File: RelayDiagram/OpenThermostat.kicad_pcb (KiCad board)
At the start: 2 copper layers, 152.5 x 101.5 mm, 90 parts, among them J1 Conn_01x08_Female, J2 Conn_01x15_Female, J3 Conn_01x15_Female, J4 Conn_01x09_Female, Q1 Q_NMOS_DGS, Q10 Q_NMOS_DGS, Q11 Q_NMOS_DGS, Q12 Q_NMOS_DGS, Q2 Q_NMOS_DGS, Q3 Q_NMOS_DGS, Q4 Q_NMOS_DGS, Q5 Q_NMOS_DGS, Q6 Q_NMOS_DGS, Q7 Q_NMOS_DGS, Q8 Q_NMOS_DGS, Q9 Q_NMOS_DGS, SW2 SW_Push, SW3 SW_Push, SW4 SW_Push, SW5 SW_Push, SW6 SW_Push, U1 PCF8574, U10 MB10S-13, U11 L7805CV, U2 LCD, U3 DHT11, U4 EE2-3TNU-L_DPDT_Relay, U5 EE2-3TNU-L_DPDT_Relay, U6 EE2-3TNU-L_DPDT_Relay, U7 EE2-3TNU-L_DPDT_Relay, U8 EE2-3TNU-L_DPDT_Relay, U9 EE2-3TNU-L_DPDT_Relay

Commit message: Change
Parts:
- moved R38 8.19 mm to (160.3, 153.9), turned to 90 degrees
- moved Q5 5.71 mm to (163.7, 149.7)
- moved R15 5.54 mm to (165.0, 128.9)
- moved R14 5.20 mm to (163.7, 154.3)
- moved R26 5.20 mm to (163.7, 151.6)
- moved R39 5.07 mm to (165.5, 125.1)
- moved D6 5.03 mm to (161.3, 125.1)
- moved Q6 3.29 mm to (161.0, 128.9), turned to 90 degrees
- moved D5 2.16 mm to (160.3, 149.5), turned to 90 degrees
- moved R27 1.76 mm to (162.8, 128.9), turned to 90 degrees
- moved U6 0.55 mm to (167.4, 145.2)
- moved R35 0.08 mm to (198.6, 129.4)
- moved Q1 0.08 mm to (189.7, 149.2)
- moved Q2 0.08 mm to (189.7, 128.4)
- moved R11 0.08 mm to (194.8, 126.6)
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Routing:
- net GND: track 39.6 -> 34.7 mm, vias 21 -> 18
- net Net-(Q2-Pad2): track 4.75 -> 0.00 mm
- net Net-(Q1-Pad2): track 4.40 -> 0.00 mm
- net Net-(D2-Pad1): track 1.72 -> 0.00 mm
- net Net-(D1-Pad1): track 1.72 -> 0.00 mm
- added copper zone on F.Cu, net +5V
- removed copper zone on F.Cu, net GND
- removed copper zone on F.Cu, net Net-(D1-Pad2)
- removed copper zone on F.Cu, net Net-(D2-Pad2)

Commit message: PCB updates
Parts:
- moved R18 30.4 mm to (129.4, 154.6), turned to 0 degrees
- moved R30 30.0 mm to (129.4, 151.9), turned to 0 degrees
- moved R31 26.0 mm to (128.7, 126.5), turned to 0 degrees
- moved R42 25.7 mm to (125.2, 154.1), turned to 90 degrees
- moved Q9 25.4 mm to (129.7, 149.7), turned to 0 degrees
- moved D12 25.2 mm to (115.8, 124.1), turned to 90 degrees
- moved R40 24.7 mm to (142.7, 153.9), turned to 90 degrees
- moved D10 24.2 mm to (132.8, 125.0), turned to 90 degrees
- moved R43 23.4 mm to (130.8, 129.7), turned to 90 degrees
- moved R19 22.6 mm to (124.3, 126.0), turned to 0 degrees
- moved D11 22.4 mm to (104.4, 149.6), turned to 90 degrees
- moved R41 22.2 mm to (150.1, 127.0)
- moved D9 21.0 mm to (125.2, 149.6), turned to 90 degrees
- moved Q10 20.4 mm to (124.5, 130.8), turned to 0 degrees
- moved U8 15.1 mm to (133.3, 145.2), turned to 90 degrees
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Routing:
- net GND: track 34.7 -> 53.7 mm, vias 18 -> 24
- net Net-(Q9-Pad2): track 0.00 -> 5.06 mm
- net Net-(Q7-Pad2): track 0.00 -> 5.06 mm
- net Net-(Q5-Pad2): track 0.00 -> 5.06 mm
- net Net-(Q3-Pad2): track 0.00 -> 5.06 mm
- net Net-(Q11-Pad2): track 0.00 -> 5.06 mm
- net Net-(Q1-Pad2): track 0.00 -> 4.93 mm
- net Net-(D9-Pad1): track 0.00 -> 1.84 mm
- net Net-(D7-Pad1): track 0.00 -> 1.84 mm
- net Net-(D5-Pad1): track 0.00 -> 1.84 mm
- net Net-(D3-Pad1): track 0.00 -> 1.84 mm
- net Net-(D11-Pad1): track 0.00 -> 1.84 mm
- net Net-(D1-Pad1): track 0.00 -> 1.84 mm
- added copper zone on F.Cu, net GND
- added copper zone on F.Cu, net Net-(D1-Pad2)
- added copper zone on F.Cu, net Net-(D11-Pad2)
- added copper zone on F.Cu, net Net-(D3-Pad2)
- added copper zone on F.Cu, net Net-(D5-Pad2)
- added copper zone on F.Cu, net Net-(D7-Pad2)
- added copper zone on F.Cu, net Net-(D9-Pad2)
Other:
- board text added: "Relays and other components here should stay on a 5 mil grid"

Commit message: relay pcb changes
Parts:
- moved D12 12.0 mm to (104.6, 128.4), turned to 270 degrees
- moved R37 9.25 mm to (175.9, 123.8), turned to 270 degrees
- moved R35 9.14 mm to (191.4, 123.8), turned to 270 degrees
- moved R19 9.08 mm to (133.0, 128.8), turned to 270 degrees
- moved R33 8.22 mm to (110.2, 125.7)
- moved D10 8.13 mm to (125.5, 128.4), turned to 270 degrees
- moved R43 7.91 mm to (125.5, 123.8), turned to 270 degrees
- moved R41 7.79 mm to (143.0, 123.8), turned to 270 degrees
- moved R21 7.65 mm to (112.1, 128.8), turned to 270 degrees
- moved R13 7.57 mm to (183.4, 128.8), turned to 270 degrees
- moved R17 7.49 mm to (150.6, 128.8), turned to 270 degrees
- moved R45 7.03 mm to (104.6, 123.8), turned to 270 degrees
- moved Q8 6.45 mm to (147.4, 128.3)
- moved Q4 6.10 mm to (180.2, 128.1)
- moved Q2 5.97 mm to (195.7, 128.1)
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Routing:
- net GND: track 53.7 -> 68.4 mm, vias 24 -> 30
- net Net-(Q8-Pad2): track 0.00 -> 5.54 mm
- net Net-(Q6-Pad2): track 0.00 -> 5.54 mm
- net Net-(Q4-Pad2): track 0.00 -> 5.49 mm
- net Net-(Q2-Pad2): track 0.00 -> 5.49 mm
- net Net-(Q12-Pad2): track 0.00 -> 5.49 mm
- net Net-(Q10-Pad2): track 0.00 -> 5.49 mm
- net Net-(D8-Pad1): track 0.00 -> 1.97 mm
- net Net-(D6-Pad1): track 0.00 -> 1.97 mm
- net Net-(D4-Pad1): track 0.00 -> 1.97 mm
- net Net-(D2-Pad1): track 0.00 -> 1.97 mm
- net Net-(D12-Pad1): track 0.00 -> 1.97 mm
- net Net-(D10-Pad1): track 0.00 -> 1.97 mm
- added copper zone on F.Cu, net Net-(D10-Pad2)
- added copper zone on F.Cu, net Net-(D12-Pad2)
- added copper zone on F.Cu, net Net-(D2-Pad2)
- added copper zone on F.Cu, net Net-(D4-Pad2)
- added copper zone on F.Cu, net Net-(D6-Pad2)
- added copper zone on F.Cu, net Net-(D8-Pad2)

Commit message: Relay updates
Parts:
- added C1: 10uF, solarcar-device:Capacitor_0805, F.Cu at (220.3, 72.0)
- moved D5 41.2 mm to (200.4, 146.7)
- moved D6 41.2 mm to (200.8, 125.6)
- moved Q5 41.2 mm to (204.9, 146.9)
- moved Q6 41.2 mm to (205.1, 125.5)
- moved R14 41.2 mm to (204.6, 151.8)
- moved R15 41.2 mm to (208.3, 126.0)
- moved R26 41.2 mm to (204.6, 149.1)
- moved R27 41.2 mm to (206.4, 122.9)
- moved R38 41.2 mm to (200.4, 151.1)
- moved R39 41.2 mm to (200.8, 121.0)
- moved U6 41.2 mm to (208.5, 142.4)
- moved R7 40.1 mm to (117.1, 103.5), turned to 0 degrees
- moved D7 39.2 mm to (181.9, 146.7)
- moved R16 39.2 mm to (186.1, 151.8)
- moved R28 39.2 mm to (186.1, 149.1)
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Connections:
- U4 pad 5: Net-(J4-Pad3) -> Net-(J4-Pad6)
- U4 pad 8: Net-(J4-Pad3) -> Net-(J4-Pad6)
- U5 pad 5: Net-(J4-Pad4) -> Net-(J4-Pad5)
- U5 pad 8: Net-(J4-Pad4) -> Net-(J4-Pad5)
- U6 pad 5: Net-(J4-Pad5) -> Net-(J4-Pad8)
- U6 pad 8: Net-(J4-Pad5) -> Net-(J4-Pad8)
- U7 pad 5: Net-(J4-Pad6) -> Net-(J4-Pad7)
- U7 pad 8: Net-(J4-Pad6) -> Net-(J4-Pad7)
- U8 pad 5: Net-(J4-Pad7) -> Net-(J4-Pad4)
- U8 pad 8: Net-(J4-Pad7) -> Net-(J4-Pad4)
- U9 pad 5: Net-(J4-Pad8) -> Net-(J4-Pad3)
- U9 pad 8: Net-(J4-Pad8) -> Net-(J4-Pad3)
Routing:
- net Net-(J3-Pad6): track 0.00 -> 127.2 mm, vias 0 -> 2
- net Net-(J3-Pad8): track 0.00 -> 108.1 mm, vias 0 -> 2
- net Net-(J3-Pad5): track 0.00 -> 103.3 mm
- net Net-(J2-Pad3): track 0.00 -> 89.2 mm, vias 0 -> 2
- net Net-(J2-Pad15): track 106.3 -> 18.8 mm, vias 4 -> 3
- net Net-(J3-Pad7): track 0.00 -> 84.2 mm
- net Net-(J2-Pad13): track 98.6 -> 23.1 mm, vias 4 -> 3
- net Net-(J3-Pad4): track 0.00 -> 70.1 mm, vias 0 -> 2
- net Net-(J2-Pad4): track 0.00 -> 64.9 mm
- net Net-(J4-Pad8): track 0.00 -> 54.6 mm
- net Net-(J4-Pad3): track 0.00 -> 52.6 mm
- net Net-(J3-Pad10): track 0.00 -> 51.1 mm, vias 0 -> 2
- net Net-(J3-Pad3): track 0.00 -> 45.9 mm
- net Net-(J4-Pad7): track 0.00 -> 39.4 mm
- net Net-(J4-Pad4): track 0.00 -> 36.6 mm
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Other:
- board size 152.5 x 101.5 mm -> 162.6 x 102.4 mm
- board text added: "Open Thermostat Rev. A ------------ Tristan Ponder Doug Basler Nick Covert"
- board text removed: "Open Thermostat Rev. A Tristan Ponder, Doug Basler, Nick Covert"

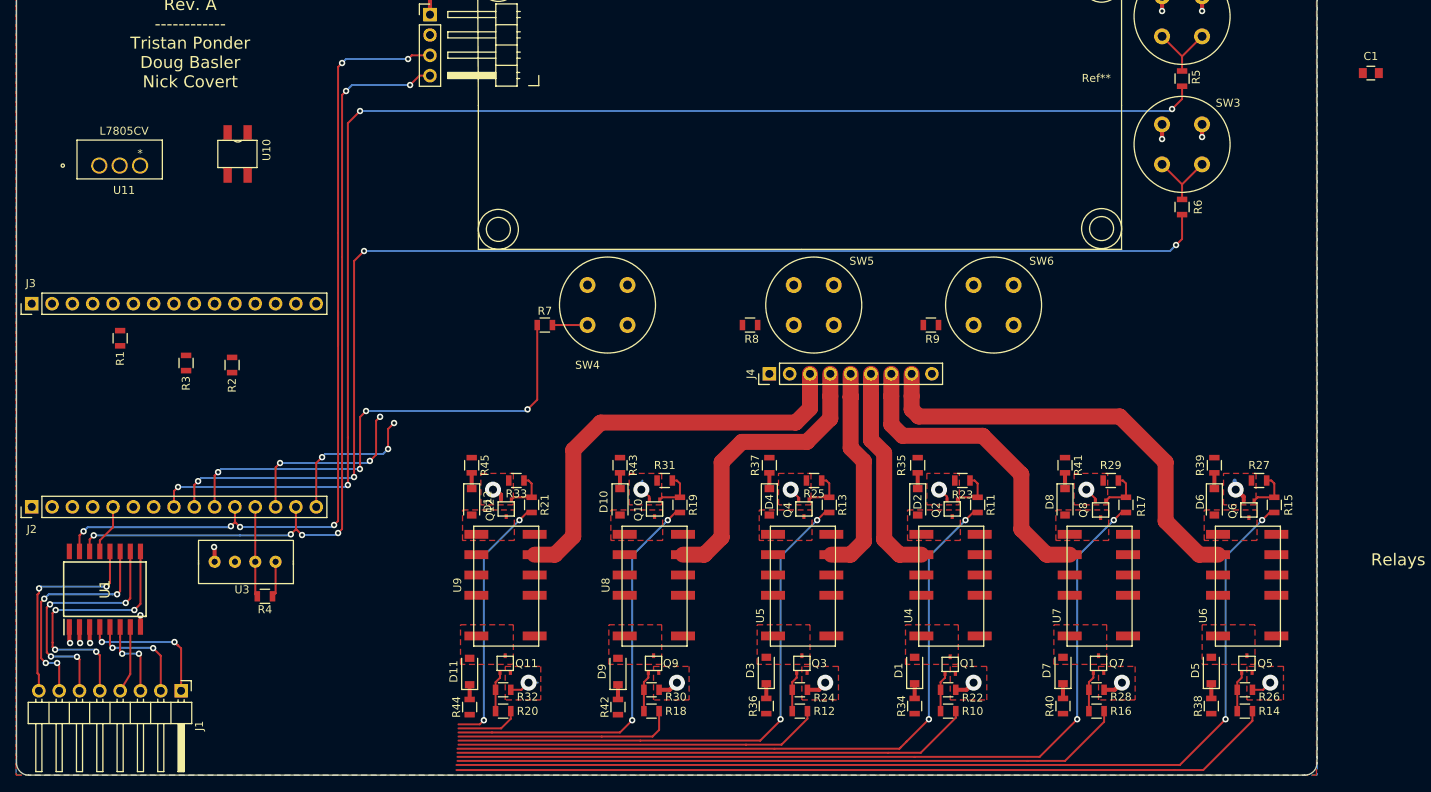
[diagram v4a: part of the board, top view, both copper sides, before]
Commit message: Major routing. Board should be nearly complete apart from review and minor changes.
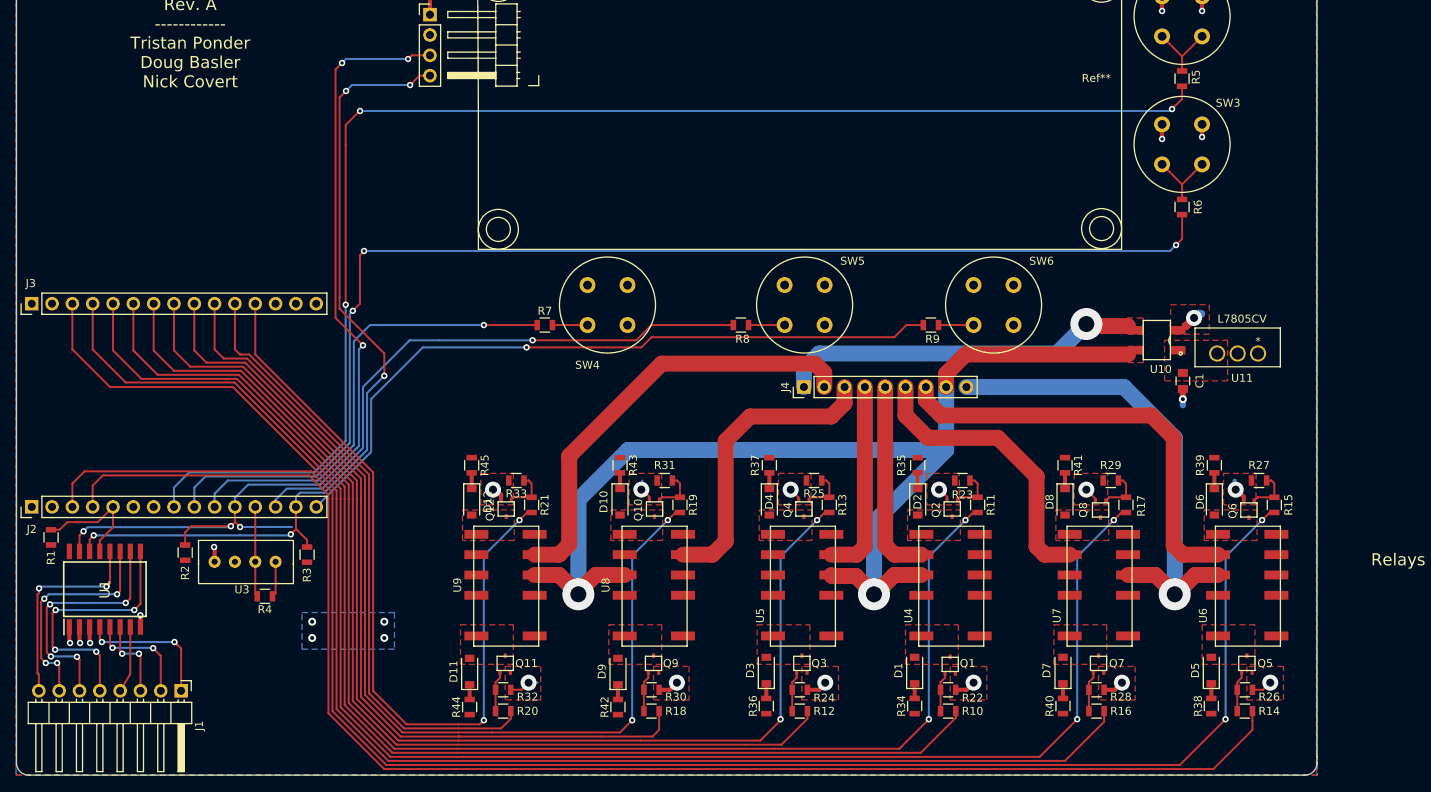
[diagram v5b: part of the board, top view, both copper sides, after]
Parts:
- moved U11 141.7 mm to (206.2, 105.5)
- moved U10 114.5 mm to (190.0, 103.6), turned to 270 degrees
- moved C1 45.1 mm to (196.8, 110.5), turned to 270 degrees
- moved R3 28.3 mm to (87.4, 132.2)
- moved R1 26.3 mm to (55.4, 130.0)
- moved R2 24.2 mm to (72.1, 132.0)
- moved J4 4.62 mm to (149.5, 111.3)
- moved R8 1.14 mm to (141.6, 103.5)
- moved SW5 1.14 mm to (147.1, 103.5)
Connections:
- J4 pad 1: /RC -> Net-(J4-Pad1)
- J4 pad 2: /R -> Net-(J4-Pad2)
- J4 pad 8: Net-(J4-Pad8) -> /R
- J4 pad 9: GND -> /RC
- R10 pad 2: Net-(J2-Pad4) -> Net-(J3-Pad5)
- R11 pad 2: Net-(J2-Pad3) -> Net-(J3-Pad6)
- R12 pad 2: Net-(J3-Pad3) -> Net-(J3-Pad7)
- R13 pad 2: Net-(J3-Pad4) -> Net-(J3-Pad8)
- R14 pad 2: Net-(J3-Pad5) -> Net-(J2-Pad4)
- R15 pad 2: Net-(J3-Pad6) -> Net-(J2-Pad3)
- R16 pad 2: Net-(J3-Pad7) -> Net-(J3-Pad3)
- R17 pad 2: Net-(J3-Pad8) -> Net-(J3-Pad4)
- U10 pad 4: Net-(U10-Pad4) -> Net-(J4-Pad1)
- U4 pad 5: Net-(J4-Pad6) -> Net-(J4-Pad5)
- U4 pad 8: Net-(J4-Pad6) -> Net-(J4-Pad5)
- U5 pad 5: Net-(J4-Pad5) -> Net-(J4-Pad4)
- U5 pad 8: Net-(J4-Pad5) -> Net-(J4-Pad4)
- U6 pad 5: Net-(J4-Pad8) -> Net-(J4-Pad7)
- U6 pad 8: Net-(J4-Pad8) -> Net-(J4-Pad7)
- U7 pad 5: Net-(J4-Pad7) -> Net-(J4-Pad6)
- U7 pad 8: Net-(J4-Pad7) -> Net-(J4-Pad6)
- U8 pad 5: Net-(J4-Pad4) -> Net-(J4-Pad3)
- U8 pad 8: Net-(J4-Pad4) -> Net-(J4-Pad3)
- U9 pad 5: Net-(J4-Pad3) -> Net-(J4-Pad2)
- U9 pad 8: Net-(J4-Pad3) -> Net-(J4-Pad2)
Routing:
- net /R: track 0.00 -> 142.0 mm, vias 0 -> 2
- net Net-(J3-Pad3): track 45.9 -> 175.3 mm
- net Net-(J3-Pad4): track 70.1 -> 196.5 mm
- net Net-(J2-Pad3): track 89.2 -> 210.0 mm
- net Net-(J2-Pad4): track 64.9 -> 183.7 mm
- net Net-(J3-Pad9): track 27.8 -> 102.7 mm
- net Net-(J3-Pad10): track 51.1 -> 123.2 mm
- net Net-(J2-Pad15): track 18.8 -> 89.2 mm, vias 3 -> 1
- net Net-(J3-Pad11): track 7.99 -> 77.3 mm
- net Net-(J3-Pad12): track 32.2 -> 99.1 mm
- net /RC: track 0.00 -> 61.5 mm, vias 0 -> 1
- net Net-(J4-Pad2): track 0.00 -> 54.8 mm
- net Net-(J4-Pad8): track 54.6 -> 0.00 mm
- net Net-(J2-Pad13): track 23.1 -> 71.6 mm, vias 3 -> 1
- net Net-(J3-Pad5): track 103.3 -> 150.7 mm
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- added copper zone on B.Cu, net +5V
- added copper zone on F.Cu, net /R
- added copper zone on F.Cu, net /V+
- added copper zone on F.Cu, net Net-(J4-Pad1)

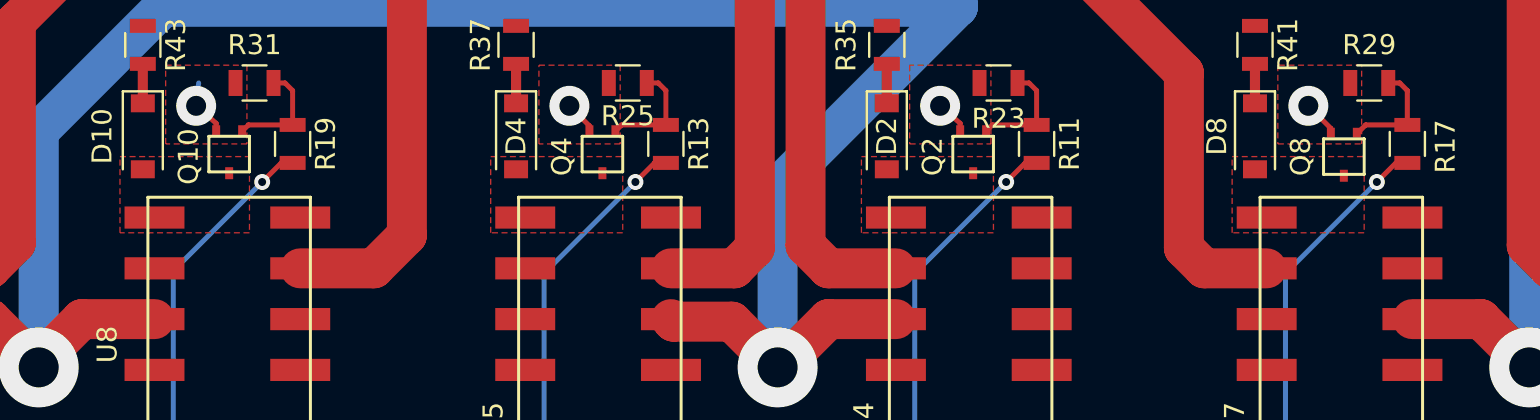
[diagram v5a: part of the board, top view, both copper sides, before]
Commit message: Fixed some relays not connected to +5V
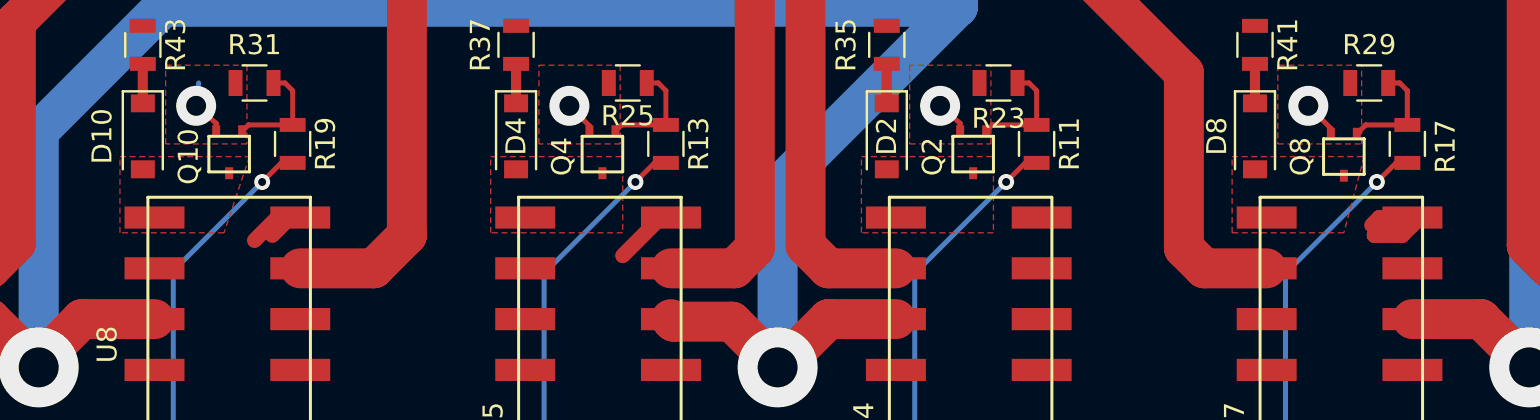
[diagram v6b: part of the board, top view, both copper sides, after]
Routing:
- net +5V: track 4.48 -> 19.2 mm
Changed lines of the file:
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@@
     (thickness 1.6)
     (drawings 25)
-    (tracks 654)
+    (tracks 667)
     (zones 0)
     (modules 91)
@@
   )
   (setup
-    (last_trace_width 0.25)
+    (last_trace_width 0.762)
     (user_trace_width 0.254)
     (user_trace_width 0.508)
@@
   (segment (start 83.439 137.028) (end 83.053 137.414) (width 0.254) (layer F.Cu) (net 59))
   (segment (start 83.439 133.096) (end 83.439 137.028) (width 0.254) (layer F.Cu) (net 59))
+  (segment (start 134.366 129.667) (end 133.223 129.667) (width 0.762) (layer F.Cu) (net 59) (status C00000))
+  (segment (start 133.223 129.667) (end 132.08 130.81) (width 0.762) (layer F.Cu) (net 59) (status 400000))
+  (segment (start 134.366 129.667) (end 133.858 129.667) (width 0.762) (layer F.Cu) (net 59) (status C00000))
+  (segment (start 133.858 129.667) (end 132.969 130.556) (width 0.762) (layer F.Cu) (net 59) (status 400000))
+  (segment (start 189.992 129.667) (end 188.976 129.667) (width 0.762) (layer F.Cu) (net 59) (status C00000))
+  (segment (start 189.484 130.556) (end 188.087 130.556) (width 0.762) (layer F.Cu) (net 59))
+  (segment (start 189.992 130.048) (end 189.484 130.556) (width 0.762) (layer F.Cu) (net 59) (status 400000))
+  (segment (start 189.992 129.667) (end 189.992 130.048) (width 0.762) (layer F.Cu) (net 59) (status C00000))
+  (segment (start 188.976 129.667) (end 188.087 130.556) (width 0.762) (layer F.Cu) (net 59) (status 400000))
+  (segment (start 189.992 129.667) (end 188.341 129.667) (width 0.762) (layer F.Cu) (net 59) (status 400000))
+  (segment (start 188.341 129.667) (end 187.96 130.048) (width 0.762) (layer F.Cu) (net 59))
+  (segment (start 152.908 129.667) (end 152.4 129.667) (width 0.762) (layer F.Cu) (net 59) (status C00000))
+  (segment (start 152.4 129.667) (end 150.495 131.572) (width 0.762) (layer F.Cu) (net 59) (status 400000))
   (segment (start 164.719 111.252) (end 164.719 112.903) (width 2) (layer F.Cu) (net 60) (status 400000))
   (segment (start 196.85 132.207) (end 201.244 132.207) (width 2) (layer F.Cu) (net 60) (status 800000))
@@
     (polygon
       (pts
-        (xy 180.975 130.429) (xy 180.975 126.619) (xy 187.579 126.619) (xy 187.579 130.429)
+        (xy 180.975 130.429) (xy 180.975 126.619) (xy 187.579 126.619) (xy 186.563 130.429)
       )
     )
@@
     (polygon
       (pts
-        (xy 125.349 130.429) (xy 125.349 126.619) (xy 131.826 126.619) (xy 131.826 130.429)
+        (xy 125.349 130.429) (xy 125.349 126.619) (xy 131.826 126.619) (xy 130.556 130.429)
       )
     )
